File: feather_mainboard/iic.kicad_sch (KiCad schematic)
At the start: 3 parts, among them J4 61300211121

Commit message: finished daughter board
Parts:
- removed R5: WRIS-RSKS_0603, Custom footprints:WRIS-RSKS_0603_REFLOW, symbol WRIS-RSKS_0603:WRIS-RSKS_0603
- added R4: 10kΩ, Custom footprints:WRIS-RSKS_0603_REFLOW, symbol WRIS-RSKS_0603:WRIS-RSKS_0603
- R3: value 10k -> 10kΩ
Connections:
- net SCL: now also J4.2, R4.1
- net SDA: now also J4.1, R3.1
- net VCC: now reaches R3.2
- net VCC: now also R4.2
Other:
- moved on the sheet: J4, R3
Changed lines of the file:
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@@
 	(generator_version "8.0")
 	(paper "A4")
-	(wire
-		(pts
-			(xy 138.43 74.93) (xy 152.4 74.93)
-		)
-		(stroke
-			(width 0)
-			(type default)
-		)
-	)
-	(wire
-		(pts
-			(xy 138.43 71.12) (xy 152.4 71.12)
-		)
-		(stroke
-			(width 0)
-			(type default)
+	(junction
+		(at 144.78 109.22)
+		(diameter 0)
+		(color 0 0 0 0)
+	)
+	(junction
+		(at 154.94 111.76)
+		(diameter 0)
+		(color 0 0 0 0)
+	)
+	(junction
+		(at 149.86 87.63)
+		(diameter 0)
+		(color 0 0 0 0)
+	)
+	(wire
+		(pts
+			(xy 154.94 87.63) (xy 149.86 87.63)
+		)
+		(stroke
+			(width 0)
+			(type default)
+		)
+	)
+	(wire
+		(pts
+			(xy 149.86 87.63) (xy 149.86 85.09)
+		)
+		(stroke
+			(width 0)
+			(type default)
+		)
+	)
+	(wire
+		(pts
+			(xy 154.94 105.41) (xy 154.94 111.76)
+		)
+		(stroke
+			(width 0)
+			(type default)
+		)
+	)
+	(wire
+		(pts
+			(xy 144.78 109.22) (xy 161.29 109.22)
+		)
+		(stroke
+			(width 0)
+			(type default)
+		)
+	)
+	(wire
+		(pts
+			(xy 154.94 90.17) (xy 154.94 87.63)
+		)
+		(stroke
+			(width 0)
+			(type default)
+		)
+	)
+	(wire
+		(pts
+			(xy 144.78 87.63) (xy 149.86 87.63)
+		)
+		(stroke
+			(width 0)
+			(type default)
+		)
+	)
+	(wire
+		(pts
+			(xy 138.43 111.76) (xy 154.94 111.76)
+		)
+		(stroke
+			(width 0)
+			(type default)
+		)
+	)
+	(wire
+		(pts
+			(xy 138.43 109.22) (xy 144.78 109.22)
+		)
+		(stroke
+			(width 0)
+			(type default)
+		)
+	)
+	(wire
+		(pts
+			(xy 144.78 105.41) (xy 144.78 109.22)
+		)
+		(stroke
+			(width 0)
+			(type default)
+		)
+	)
+	(wire
+		(pts
+			(xy 144.78 90.17) (xy 144.78 87.63)
+		)
+		(stroke
+			(width 0)
+			(type default)
+		)
+	)
+	(wire
+		(pts
+			(xy 154.94 111.76) (xy 161.29 111.76)
+		)
+		(stroke
+			(width 0)
+			(type default)
+		)
+	)
+	(global_label "VCC"
+		(shape bidirectional)
+		(at 149.86 85.09 90)
+		(fields_autoplaced yes)
+		(effects
+			(font
+				(size 1.27 1.27)
+			)
+			(justify left)
+		)
+		(property "Intersheetrefs" "${INTERSHEET_REFS}"
+			(at 149.86 77.3649 90)
+			(effects
+				(font
+					(size 1.27 1.27)
+				)
+				(justify left)
+				(hide yes)
+			)
 		)
 	)
 	(hierarchical_label "SCL"
 		(shape bidirectional)
-		(at 138.43 74.93 180)
+		(at 138.43 111.76 180)
 		(fields_autoplaced yes)
 		(effects
@@
 	(hierarchical_label "SDA"
 		(shape bidirectional)
-		(at 138.43 71.12 180)
+		(at 138.43 109.22 180)
 		(fields_autoplaced yes)
 		(effects
@@
 	(symbol
 		(lib_id "6130XX11121_61300211121:6130XX11121_61300211121")
-		(at 165.1 74.93 270)
+		(at 166.37 111.76 270)
 		(unit 1)
 		(exclude_from_sim no)
@@
 		(on_board yes)
 		(dnp no)
-		(fields_autoplaced yes)
 		(property "Reference" "J4"
-			(at 166.37 73.6599 90)
+			(at 163.83 106.934 90)
 			(effects
 				(font
@@
 		)
 		(property "Value" "61300211121"
-			(at 165.1 74.93 0)
+			(at 166.37 111.76 0)
 			(effects
 				(font
@@
 		)
 		(property "Footprint" "Custom footprints:61300211121"
-			(at 165.1 74.93 0)
+			(at 166.37 111.76 0)
 			(effects
 				(font
@@
 		)
 		(property "Datasheet" ""
-			(at 165.1 74.93 0)
+			(at 166.37 111.76 0)
 			(effects
 				(font
@@
 		)
 		(property "Description" ""
-			(at 165.1 74.93 0)
+			(at 166.37 111.76 0)
 			(effects
 				(font
@@
 		)
 		(property "ROWS" "Single"
-			(at 165.1 74.93 0)
+			(at 166.37 111.76 0)
 			(effects
 				(font
@@
 		)
 		(property "GENDER" "Pin Header"
-			(at 165.1 74.93 0)
+			(at 166.37 111.76 0)
 			(effects
 				(font
@@
 		)
 		(property "MOUNT" "THT"
-			(at 165.1 74.93 0)
+			(at 166.37 111.76 0)
 			(effects
 				(font
@@
 		)
 		(property "IR" "3A"
-			(at 165.1 74.93 0)
+			(at 166.37 111.76 0)
 			(effects
 				(font
@@
 		)
 		(property "PACKAGING" "Bag"
-			(at 165.1 74.93 0)
+			(at 166.37 111.76 0)
 			(effects
 				(font
@@
 		)
 		(property "PINS" "2"
-			(at 165.1 74.93 0)
+			(at 166.37 111.76 0)
 			(effects
 				(font
@@
 		)
 		(property "DATASHEET-URL" "https://www.we-online.com/redexpert/spec/61300211121?ae"
-			(at 165.1 74.93 0)
+			(at 166.37 111.76 0)
 			(effects
 				(font
@@
 		)
 		(property "PITCH" "2.54mm"
-			(at 165.1 74.93 0)
+			(at 166.37 111.76 0)
 			(effects
 				(font
@@
 		)
 		(property "PART-NUMBER" "61300211121"
-			(at 165.1 74.93 0)
+			(at 166.37 111.76 0)
 			(effects
 				(font
@@
 		)
 		(property "TYPE" "Straight"
-			(at 165.1 74.93 0)
+			(at 166.37 111.76 0)
 			(effects
 				(font
@@
 	(symbol
 		(lib_id "WRIS-RSKS_0603:WRIS-RSKS_0603")
-		(at 180.34 55.88 90)
+		(at 154.94 97.79 90)
 		(unit 1)
 		(exclude_from_sim no)
@@
 		(on_board yes)
 		(dnp no)
-		(fields_autoplaced yes)
-		(property "Reference" "R5"
-			(at 182.88 54.6099 90)
+		(property "Reference" "R4"
+			(at 156.464 96.774 90)
 			(effects
 				(font
@@
 			)
 		)
-		(property "Value" "WRIS-RSKS_0603"
-			(at 182.88 57.1499 90)
+		(property "Value" "10kΩ"
+			(at 156.464 98.552 90)
 			(effects
 				(font
@@
 		)
 		(property "Footprint" "Custom footprints:WRIS-RSKS_0603_REFLOW"
-			(at 180.34 55.88 0)
+			(at 154.94 97.79 0)
 			(effects
 				(font
@@
 		)
 		(property "Datasheet" ""
-			(at 180.34 55.88 0)
+			(at 154.94 97.79 0)
 			(effects
 				(font
@@
 		)
 		(property "Description" ""
-			(at 180.34 55.88 0)
-			(effects
-				(font
-					(size 1.27 1.27)
-				)
-				(hide yes)
-			)
+			(at 154.94 97.79 0)
+			(effects
+				(font
+					(size 1.27 1.27)
+				)
+				(hide yes)
+			)
+		)
+		(pin "2"
 		)
 		(pin "1"
-		)
-		(pin "2"
 		)
 		(instances
 			(project "feather_mainboard"
 				(path "/e1e12730-ab4f-45db-8b66-c1e0f78e2f00/9211cf2c-296b-49a8-984c-d8eee48b72b3"
-					(reference "R5")
+					(reference "R4")
 					(unit 1)
 				)
@@
 	(symbol
 		(lib_id "WRIS-RSKS_0603:WRIS-RSKS_0603")
-		(at 152.4 55.88 90)
+		(at 144.78 97.79 90)
 		(unit 1)
 		(exclude_from_sim no)
@@
 		(on_board yes)
 		(dnp no)
-		(fields_autoplaced yes)
 		(property "Reference" "R3"
-			(at 154.94 54.6099 90)
+			(at 146.304 96.774 90)
 			(effects
 				(font
@@
 			)
 		)
-		(property "Value" "10k"
-			(at 154.94 57.1499 90)
+		(property "Value" "10kΩ"
+			(at 146.304 98.552 90)
 			(effects
 				(font
@@
 		)
 		(property "Footprint" "Custom footprints:WRIS-RSKS_0603_REFLOW"
-			(at 152.4 55.88 0)
+			(at 144.78 97.79 0)
 			(effects
 				(font
@@
 		)
 		(property "Datasheet" ""
-			(at 152.4 55.88 0)
+			(at 144.78 97.79 0)
 			(effects
 				(font
@@
 		)
 		(property "Description" ""
-			(at 152.4 55.88 0)
-			(effects
-				(font
+			(at 144.78 97.79 0)
+			(effects
+				(font

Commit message: finished mainboard design, need to do the routing
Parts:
- renumbered J4 to J6, R3 to R1_3, R4 to R1_4
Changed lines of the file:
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@@
 			(font
 				(size 1.27 1.27)
-				(bold yes)
 			)
 			(justify right)
@@
 			(font
 				(size 1.27 1.27)
-				(bold yes)
 			)
 			(justify right)
@@
 		(on_board yes)
 		(dnp no)
-		(property "Reference" "J4"
+		(property "Reference" "J6"
 			(at 163.83 106.934 90)
 			(effects
@@
 		(instances
 			(project "feather_mainboard"
-				(path "/e1e12730-ab4f-45db-8b66-c1e0f78e2f00/9211cf2c-296b-49a8-984c-d8eee48b72b3"
-					(reference "J4")
+				(path "/e1e12730-ab4f-45db-8b66-c1e0f78e2f00/ff9ad5fa-00ba-4ea3-956b-8f18c92a633c"
+					(reference "J6")
 					(unit 1)
 				)
@@
 		(on_board yes)
 		(dnp no)
-		(property "Reference" "R4"
+		(property "Reference" "R1_4"
 			(at 156.464 96.774 90)
 			(effects
@@
 		(instances
 			(project "feather_mainboard"
-				(path "/e1e12730-ab4f-45db-8b66-c1e0f78e2f00/9211cf2c-296b-49a8-984c-d8eee48b72b3"
-					(reference "R4")
+				(path "/e1e12730-ab4f-45db-8b66-c1e0f78e2f00/ff9ad5fa-00ba-4ea3-956b-8f18c92a633c"
+					(reference "R1_4")
 					(unit 1)
 				)
@@
 		(on_board yes)
 		(dnp no)
-		(property "Reference" "R3"
+		(property "Reference" "R1_3"
 			(at 146.304 96.774 90)
 			(effects
@@
 		(instances
 			(project "feather_mainboard"
-				(path "/e1e12730-ab4f-45db-8b66-c1e0f78e2f00/9211cf2c-296b-49a8-984c-d8eee48b72b3"
-					(reference "R3")
+				(path "/e1e12730-ab4f-45db-8b66-c1e0f78e2f00/ff9ad5fa-00ba-4ea3-956b-8f18c92a633c"
+					(reference "R1_3")
 					(unit 1)
 				)

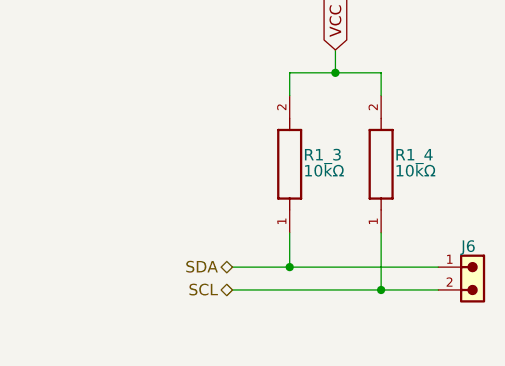
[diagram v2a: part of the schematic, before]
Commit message: changed the connector on the daughter board
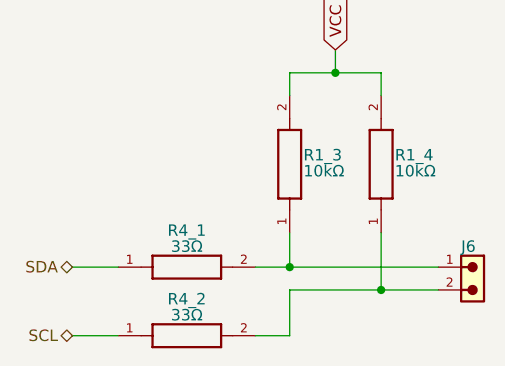
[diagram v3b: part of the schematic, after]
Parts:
- added R4_1, R4_2: 33Ω, Custom footprints:WRIS-RSKS_0603_REFLOW, symbol WRIS-RSKS_0603:WRIS-RSKS_0603
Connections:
- net SCL: now also R4_2.1; no longer J6.2, R1_4.1
- net SDA: now also R4_1.1; no longer J6.1, R1_3.1
- new net: J6.1, R1_3.1, R4_1.2
- new net: J6.2, R1_4.1, R4_2.2
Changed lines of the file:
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@@
+	(wire
+		(pts
+			(xy 144.78 116.84) (xy 140.97 116.84)
+		)
+		(stroke
+			(width 0)
+			(type default)
+		)
+	)
 	(wire
 		(pts
@@
 	(wire
 		(pts
+			(xy 120.65 116.84) (xy 125.73 116.84)
+		)
+		(stroke
+			(width 0)
+			(type default)
+		)
+	)
+	(wire
+		(pts
+			(xy 120.65 109.22) (xy 125.73 109.22)
+		)
+		(stroke
+			(width 0)
+			(type default)
+		)
+	)
+	(wire
+		(pts
+			(xy 144.78 109.22) (xy 161.29 109.22)
+		)
+		(stroke
+			(width 0)
+			(type default)
+		)
+	)
+	(wire
+		(pts
+			(xy 140.97 109.22) (xy 144.78 109.22)
+		)
+		(stroke
+			(width 0)
+			(type default)
+		)
+	)
+	(wire
+		(pts
+			(xy 144.78 111.76) (xy 144.78 116.84)
+		)
+		(stroke
+			(width 0)
+			(type default)
+		)
+	)
+	(wire
+		(pts
+			(xy 154.94 90.17) (xy 154.94 87.63)
+		)
+		(stroke
+			(width 0)
+			(type default)
+		)
+	)
+	(wire
+		(pts
+			(xy 144.78 87.63) (xy 149.86 87.63)
+		)
+		(stroke
+			(width 0)
+			(type default)
+		)
+	)
+	(wire
+		(pts
+			(xy 144.78 105.41) (xy 144.78 109.22)
+		)
+		(stroke
+			(width 0)
+			(type default)
+		)
+	)
+	(wire
+		(pts
 			(xy 154.94 105.41) (xy 154.94 111.76)
 		)
@@
 	(wire
 		(pts
-			(xy 144.78 109.22) (xy 161.29 109.22)
-		)
-		(stroke
-			(width 0)
-			(type default)
-		)
-	)
-	(wire
-		(pts
-			(xy 154.94 90.17) (xy 154.94 87.63)
-		)
-		(stroke
-			(width 0)
-			(type default)
-		)
-	)
-	(wire
-		(pts
-			(xy 144.78 87.63) (xy 149.86 87.63)
-		)
-		(stroke
-			(width 0)
-			(type default)
-		)
-	)
-	(wire
-		(pts
-			(xy 138.43 111.76) (xy 154.94 111.76)
-		)
-		(stroke
-			(width 0)
-			(type default)
-		)
-	)
-	(wire
-		(pts
-			(xy 138.43 109.22) (xy 144.78 109.22)
-		)
-		(stroke
-			(width 0)
-			(type default)
-		)
-	)
-	(wire
-		(pts
-			(xy 144.78 105.41) (xy 144.78 109.22)
-		)
-		(stroke
-			(width 0)
-			(type default)
-		)
-	)
-	(wire
-		(pts
 			(xy 144.78 90.17) (xy 144.78 87.63)
 		)
@@
 		(pts
 			(xy 154.94 111.76) (xy 161.29 111.76)
+		)
+		(stroke
+			(width 0)
+			(type default)
+		)
+	)
+	(wire
+		(pts
+			(xy 144.78 111.76) (xy 154.94 111.76)
 		)
 		(stroke
@@
 	(hierarchical_label "SCL"
 		(shape bidirectional)
-		(at 138.43 111.76 180)
+		(at 120.65 116.84 180)
 		(fields_autoplaced yes)
 		(effects
@@
 	(hierarchical_label "SDA"
 		(shape bidirectional)
-		(at 138.43 109.22 180)
+		(at 120.65 109.22 180)
 		(fields_autoplaced yes)
 		(effects
@@
 	(symbol
 		(lib_id "WRIS-RSKS_0603:WRIS-RSKS_0603")
+		(at 133.35 109.22 0)
+		(unit 1)
+		(exclude_from_sim no)
+		(in_bom yes)
+		(on_board yes)
+		(dnp no)
+		(property "Reference" "R4_1"
+			(at 133.35 105.156 0)
+			(effects
+				(font
+					(size 1.27 1.27)
+				)
+			)
+		)
+		(property "Value" "33Ω"
+			(at 133.35 106.934 0)
+			(effects
+				(font
+					(size 1.27 1.27)
+				)
+			)
+		)
+		(property "Footprint" "Custom footprints:WRIS-RSKS_0603_REFLOW"
+			(at 133.35 109.22 0)
+			(effects
+				(font
+					(size 1.27 1.27)
+				)
+				(hide yes)
+			)
+		)
+		(property "Datasheet" ""
+			(at 133.35 109.22 0)
+			(effects
+				(font
+					(size 1.27 1.27)
+				)
+				(hide yes)
+			)
+		)
+		(property "Description" ""
+			(at 133.35 109.22 0)
+			(effects
+				(font
+					(size 1.27 1.27)
+				)
+				(hide yes)
+			)
+		)
+		(pin "1"
+		)
+		(pin "2"
+		)
+		(instances
+			(project "feather_mainboard"
+				(path "/e1e12730-ab4f-45db-8b66-c1e0f78e2f00/ff9ad5fa-00ba-4ea3-956b-8f18c92a633c"
+					(reference "R4_1")
+					(unit 1)
+				)
+			)
+		)
+	)
+	(symbol
+		(lib_id "WRIS-RSKS_0603:WRIS-RSKS_0603")
 		(at 154.94 97.79 90)
 		(unit 1)
@@
 					(unit 1)
 				)
+			)
+		)
+	)
+	(symbol
+		(lib_id "WRIS-RSKS_0603:WRIS-RSKS_0603")
+		(at 133.35 116.84 0)
+		(unit 1)
+		(exclude_from_sim no)
+		(in_bom yes)
+		(on_board yes)
+		(dnp no)
+		(property "Reference" "R4_2"
+			(at 133.35 112.776 0)
+			(effects
+				(font
+					(size 1.27 1.27)
+				)
+			)
+		)
+		(property "Value" "33Ω"
+			(at 133.35 114.554 0)
+			(effects
+				(font
+					(size 1.27 1.27)
+				)
+			)
+		)
+		(property "Footprint" "Custom footprints:WRIS-RSKS_0603_REFLOW"
+			(at 133.35 116.84 0)
+			(effects
+				(font
+					(size 1.27 1.27)
+				)
+				(hide yes)
+			)
+		)
+		(property "Datasheet" ""
+			(at 133.35 116.84 0)
+			(effects
+				(font
+					(size 1.27 1.27)
+				)
+				(hide yes)
+			)
+		)
+		(property "Description" ""
+			(at 133.35 116.84 0)
+			(effects
+				(font
+					(size 1.27 1.27)
+				)
+				(hide yes)
+			)
+		)
+		(pin "1"
+		)
+		(pin "2"
+		)
+		(instances
+			(project "feather_mainboard"
+				(path "/e1e12730-ab4f-45db-8b66-c1e0f78e2f00/ff9ad5fa-00ba-4ea3-956b-8f18c92a633c"
+					(reference "R4_2")
+					(unit 1)
+				)

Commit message: finished mainboard and daughterboard
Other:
- moved on the sheet: J6
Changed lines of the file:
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@@
 	)
 	(junction
-		(at 154.94 111.76)
+		(at 154.94 114.3)
 		(diameter 0)
 		(color 0 0 0 0)
@@
 	(wire
 		(pts
-			(xy 144.78 109.22) (xy 161.29 109.22)
+			(xy 144.78 111.76) (xy 161.29 111.76)
 		)
 		(stroke
@@
 	(wire
 		(pts
-			(xy 144.78 111.76) (xy 144.78 116.84)
+			(xy 144.78 114.3) (xy 144.78 116.84)
 		)
 		(stroke
@@
 	(wire
 		(pts
-			(xy 154.94 105.41) (xy 154.94 111.76)
+			(xy 144.78 111.76) (xy 144.78 109.22)
+		)
+		(stroke
+			(width 0)
+			(type default)
+		)
+	)
+	(wire
+		(pts
+			(xy 154.94 105.41) (xy 154.94 114.3)
 		)
 		(stroke
@@
 	(wire
 		(pts
-			(xy 154.94 111.76) (xy 161.29 111.76)
-		)
-		(stroke
-			(width 0)
-			(type default)
-		)
-	)
-	(wire
-		(pts
-			(xy 144.78 111.76) (xy 154.94 111.76)
+			(xy 154.94 114.3) (xy 161.29 114.3)
+		)
+		(stroke
+			(width 0)
+			(type default)
+		)
+	)
+	(wire
+		(pts
+			(xy 144.78 114.3) (xy 154.94 114.3)
 		)
 		(stroke
@@
 	(symbol
 		(lib_id "6130XX11121_61300211121:6130XX11121_61300211121")
-		(at 166.37 111.76 270)
+		(at 166.37 114.3 270)
 		(unit 1)
 		(exclude_from_sim no)
@@
 		(dnp no)
 		(property "Reference" "J6"
-			(at 163.83 106.934 90)
+			(at 163.83 109.474 90)
 			(effects
 				(font
@@
 		)
 		(property "Value" "61300211121"
-			(at 166.37 111.76 0)
+			(at 166.37 114.3 0)
 			(effects
 				(font
@@
 		)
 		(property "Footprint" "Custom footprints:61300211121"
-			(at 166.37 111.76 0)
+			(at 166.37 114.3 0)
 			(effects
 				(font
@@
 		)
 		(property "Datasheet" ""
-			(at 166.37 111.76 0)
+			(at 166.37 114.3 0)
 			(effects
 				(font
@@
 		)
 		(property "Description" ""
-			(at 166.37 111.76 0)
+			(at 166.37 114.3 0)
 			(effects
 				(font
@@
 		)
 		(property "ROWS" "Single"
-			(at 166.37 111.76 0)
+			(at 166.37 114.3 0)
 			(effects
 				(font
@@
 		)
 		(property "GENDER" "Pin Header"
-			(at 166.37 111.76 0)
+			(at 166.37 114.3 0)
 			(effects
 				(font
@@
 		)
 		(property "MOUNT" "THT"
-			(at 166.37 111.76 0)
+			(at 166.37 114.3 0)
 			(effects
 				(font
@@
 		)
 		(property "IR" "3A"
-			(at 166.37 111.76 0)
+			(at 166.37 114.3 0)
 			(effects
 				(font
@@
 		)
 		(property "PACKAGING" "Bag"
-			(at 166.37 111.76 0)
+			(at 166.37 114.3 0)
 			(effects
 				(font
@@
 		)
 		(property "PINS" "2"
-			(at 166.37 111.76 0)
+			(at 166.37 114.3 0)
 			(effects
 				(font
@@
 		)
 		(property "DATASHEET-URL" "https://www.we-online.com/redexpert/spec/61300211121?ae"
-			(at 166.37 111.76 0)
+			(at 166.37 114.3 0)
 			(effects
 				(font
@@
 		)
 		(property "PITCH" "2.54mm"
-			(at 166.37 111.76 0)
+			(at 166.37 114.3 0)
 			(effects
 				(font
@@
 		)
 		(property "PART-NUMBER" "61300211121"
-			(at 166.37 111.76 0)
+			(at 166.37 114.3 0)
 			(effects
 				(font
@@
 		)
 		(property "TYPE" "Straight"
-			(at 166.37 111.76 0)
-			(effects
-				(font
+			(at 166.37 114.3 0)
+			(effects
+				(font

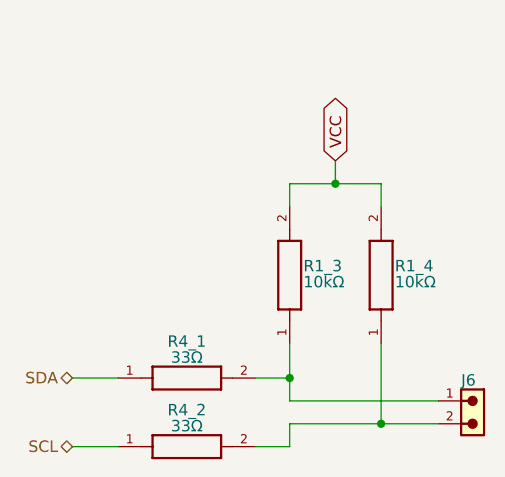
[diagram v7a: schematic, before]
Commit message: Updated the mainboard: removed unnecessary pull-ups on SD card lines; connected IIC pull-ups to enable circuit; cleaned up schematic
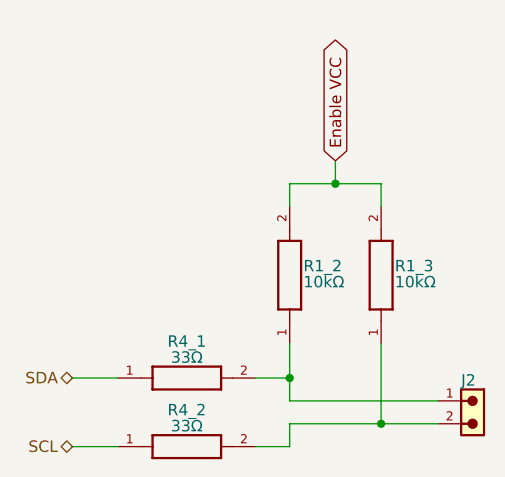
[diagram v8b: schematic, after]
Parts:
- renumbered J6 to J2, R1_3 to R1_2, R1_4 to R1_3
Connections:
- net VCC renamed Enable VCC
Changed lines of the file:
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@@
 		)
 	)
-	(global_label "VCC"
+	(global_label "Enable VCC"
 		(shape bidirectional)
 		(at 149.86 85.09 90)
@@
 		)
 		(property "Intersheetrefs" "${INTERSHEET_REFS}"
-			(at 149.86 77.3649 90)
+			(at 149.86 70.0475 90)
 			(effects
 				(font
@@
 		(shape bidirectional)
 		(at 120.65 116.84 180)
+		(fields_autoplaced yes)
 		(effects
 			(font
@@
 		(shape bidirectional)
 		(at 120.65 109.22 180)
+		(fields_autoplaced yes)
 		(effects
 			(font
@@
 		(on_board yes)
 		(dnp no)
-		(property "Reference" "J6"
+		(property "Reference" "J2"
 			(at 163.83 109.474 90)
 			(effects
@@
 		(instances
 			(project "feather_mainboard"
-				(path "/e1e12730-ab4f-45db-8b66-c1e0f78e2f00/ff9ad5fa-00ba-4ea3-956b-8f18c92a633c"
-					(reference "J6")
+				(path "/e1e12730-ab4f-45db-8b66-c1e0f78e2f00/0812b1ca-5944-46c7-9dbb-757ca60cf3f6"
+					(reference "J2")
 					(unit 1)
 				)
@@
 		(instances
 			(project "feather_mainboard"
-				(path "/e1e12730-ab4f-45db-8b66-c1e0f78e2f00/ff9ad5fa-00ba-4ea3-956b-8f18c92a633c"
+				(path "/e1e12730-ab4f-45db-8b66-c1e0f78e2f00/0812b1ca-5944-46c7-9dbb-757ca60cf3f6"
 					(reference "R4_1")
 					(unit 1)
@@
 		(on_board yes)
 		(dnp no)
-		(property "Reference" "R1_4"
+		(property "Reference" "R1_3"
 			(at 156.464 96.774 90)
 			(effects
@@
 		(instances
 			(project "feather_mainboard"
-				(path "/e1e12730-ab4f-45db-8b66-c1e0f78e2f00/ff9ad5fa-00ba-4ea3-956b-8f18c92a633c"
-					(reference "R1_4")
+				(path "/e1e12730-ab4f-45db-8b66-c1e0f78e2f00/0812b1ca-5944-46c7-9dbb-757ca60cf3f6"
+					(reference "R1_3")
 					(unit 1)
 				)
@@
 		(on_board yes)
 		(dnp no)
-		(property "Reference" "R1_3"
+		(property "Reference" "R1_2"
 			(at 146.304 96.774 90)
 			(effects
@@
 		(instances
 			(project "feather_mainboard"
-				(path "/e1e12730-ab4f-45db-8b66-c1e0f78e2f00/ff9ad5fa-00ba-4ea3-956b-8f18c92a633c"
-					(reference "R1_3")
+				(path "/e1e12730-ab4f-45db-8b66-c1e0f78e2f00/0812b1ca-5944-46c7-9dbb-757ca60cf3f6"
+					(reference "R1_2")
 					(unit 1)
 				)
@@
 		(instances
 			(project "feather_mainboard"
-				(path "/e1e12730-ab4f-45db-8b66-c1e0f78e2f00/ff9ad5fa-00ba-4ea3-956b-8f18c92a633c"
+				(path "/e1e12730-ab4f-45db-8b66-c1e0f78e2f00/0812b1ca-5944-46c7-9dbb-757ca60cf3f6"
 					(reference "R4_2")
 					(unit 1)
